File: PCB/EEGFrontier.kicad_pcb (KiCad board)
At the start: 2 copper layers, 55 x 41.5 mm, 33 parts, among them J1 Conn_01x08_Pin, SW1 SW_Push, U1 102010428, U2 ADS1299-4PAGR

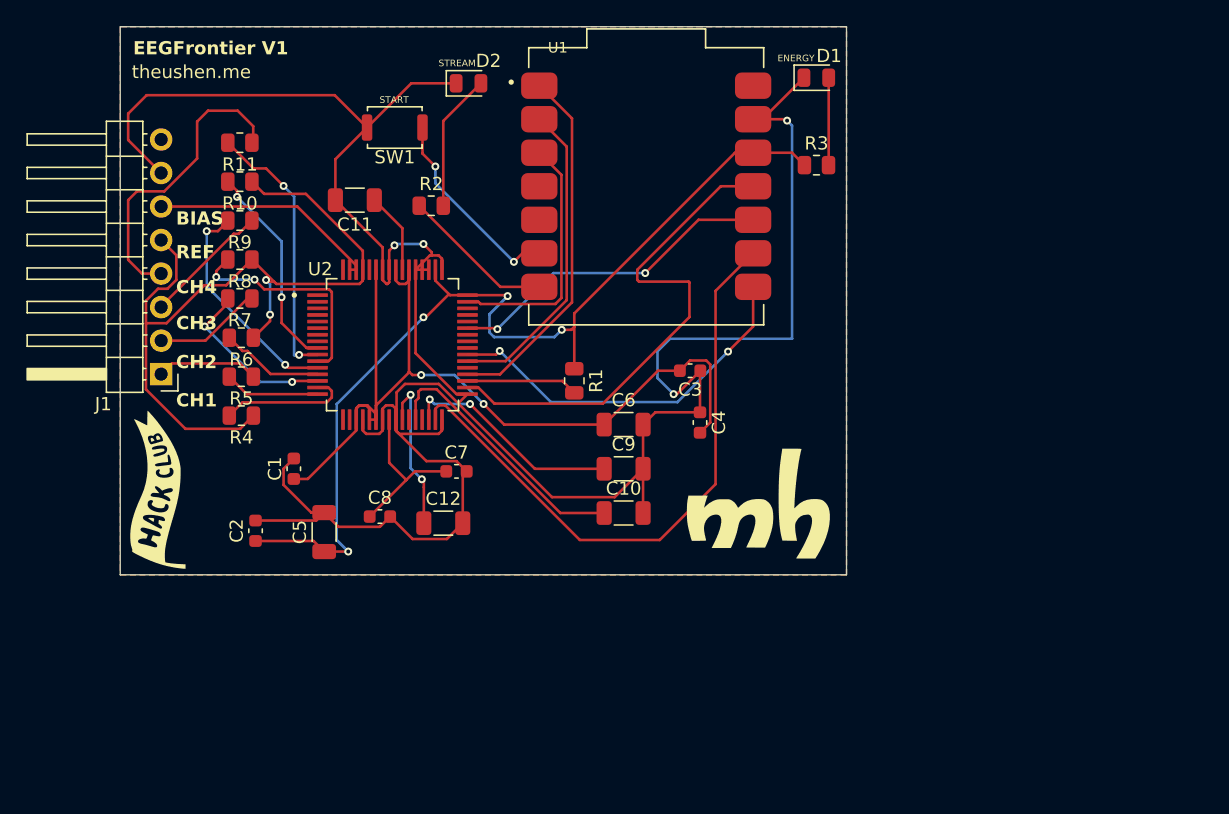
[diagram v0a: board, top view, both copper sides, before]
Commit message: feat(hw): launch EEGFrontier V2 with ADS1299IPAGR and 8-channel PCB update
- migrate analog front-end from ADS1299-4PAGR (V1) to ADS1299IPAGR (V2)
- expand hardware target from 4 EEG channels to 8 channels
- apply PCB noise-reduction rework:
  - reduce direct GND trace routing in sensitive analog areas
  - adopt curved track routing for cleaner analog paths
- update KiCad design artifacts (PCB/SCH) and generated fabrication outputs
- add V2 hardware assets (3D front/back, PCB view)
- refresh README with V1 vs V2 comparisons and updated project status

TODO (next steps):
- update BOM for V2 components and pricing
- update/validate firmware for V2 hardware revision

Refs #4
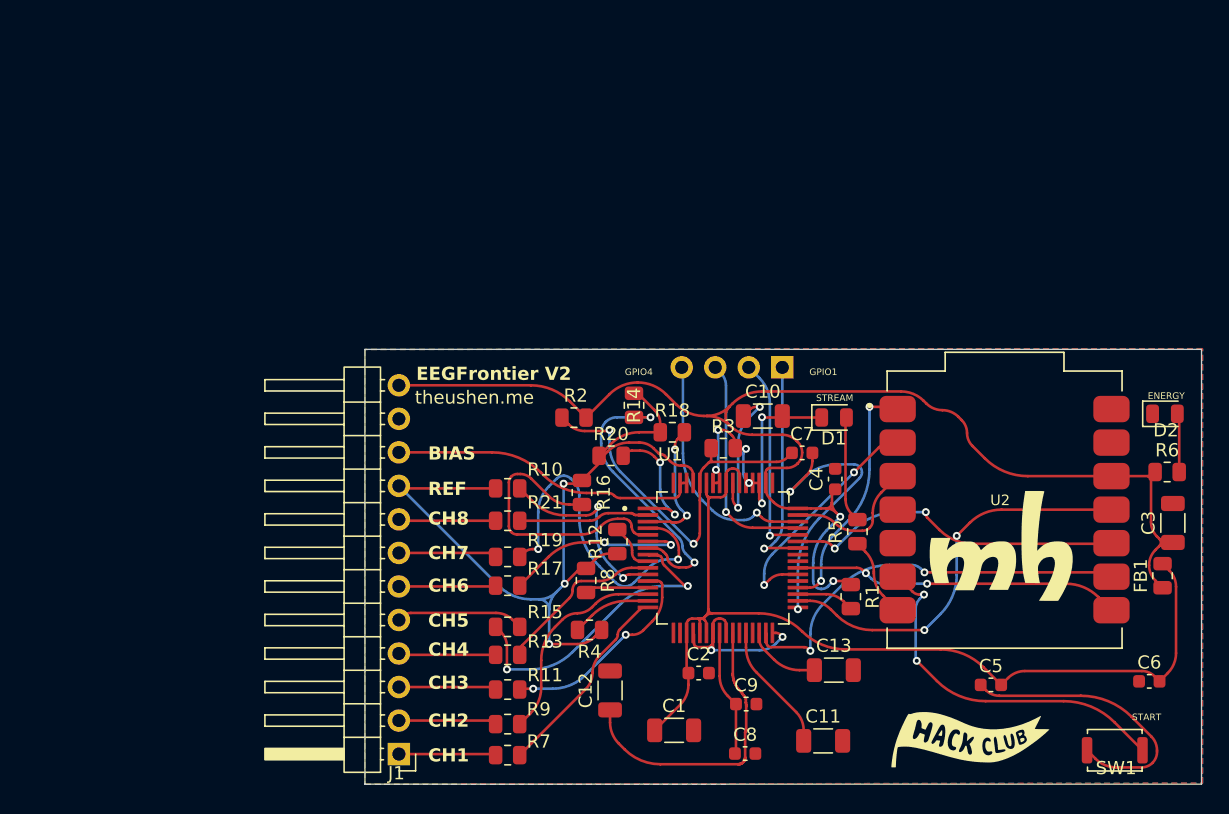
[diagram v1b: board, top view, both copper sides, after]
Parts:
- removed G*** (x4): LOGO, LOGO
- added C13: 10µF, Capacitor_SMD:C_1206_3216Metric, F.Cu at (161.1, 109.8)
- added FB1: 600Ω 100 MHz, Resistor_SMD:R_0805_2012Metric, F.Cu at (186.0, 102.6)
- added G1: LOGO, LOGO, F.Cu at (173.9, 101.6)
- added G2: LOGO, LOGO, B.Cu at (173.4, 103.2)
- added G3: LOGO, LOGO, B.Cu at (141.1, 104.0)
- added G4: LOGO, LOGO, F.Cu at (171.4, 115.0)
- added J2: Expansion, Connector_PinHeader_2.54mm:PinHeader_1x04_P2.54mm_Horizontal, B.Cu at (157.2, 86.8)
- added R12: 100k, Resistor_SMD:R_0805_2012Metric, F.Cu at (144.7, 100.0)
- added R13: 100k, Resistor_SMD:R_0805_2012Metric, F.Cu at (136.4, 108.6)
- added R14: 100k, Resistor_SMD:R_0805_2012Metric, F.Cu at (145.9, 89.7)
- added R15: 100k, Resistor_SMD:R_0805_2012Metric, F.Cu at (136.4, 106.5)
- added R16: 100k, Resistor_SMD:R_0805_2012Metric, F.Cu at (142.0, 96.3)
- added R17: 100k, Resistor_SMD:R_0805_2012Metric, F.Cu at (136.4, 103.4)
- added R18: 100k, Resistor_SMD:R_0805_2012Metric, F.Cu at (148.8, 91.7)
- added R19: 100k, Resistor_SMD:R_0805_2012Metric, F.Cu at (136.4, 101.2)
- added R20: 100k, Resistor_SMD:R_0805_2012Metric, F.Cu at (144.2, 93.5)
- added R21: 100k, Resistor_SMD:R_0805_2012Metric, F.Cu at (136.4, 98.4)
- C1, C3: value 100nF -> 10µF; footprint Capacitor_SMD:C_0603_1608Metric -> Capacitor_SMD:C_1206_3216Metric
- C5, C6, C9: value 10µF -> 100nF; footprint Capacitor_SMD:C_1206_3216Metric -> Capacitor_SMD:C_0603_1608Metric
- C7: value 100nF -> 1µF
- J1: value Conn_01x08_Pin -> Conn_01x12_Pin; footprint Connector_PinHeader_2.54mm:PinHeader_1x08_P2.54mm_Horizontal -> Connector_PinHeader_2.54mm:PinHeader_1x12_P2.54mm_Horizontal
- R2, R3: value 1kΩ -> 10k
- R5, R6: value 100k -> 1kΩ
- U1: value 102010428 -> ADS1299IPAGR; footprint OPL:MODULE_102010428 -> OPL:QFP50P1200X1200X120-64N
- U2: value ADS1299-4PAGR -> 102010428; footprint OPL:QFP50P1200X1200X120-64N -> OPL:MODULE_102010428
- moved SW1 72.1 mm to (182.3, 115.8)
- moved R6 70.9 mm to (186.3, 94.8), turned to 0 degrees
- moved D2 58.4 mm to (186.2, 90.3)
- moved C11 54.2 mm to (160.3, 115.1), turned to 0 degrees
- moved C5 51.8 mm to (173.0, 110.9), turned to 0 degrees
- moved R5 48.1 mm to (162.9, 99.3), turned to 90 degrees
- moved U2 48.0 mm to (174.0, 97.6)
- moved R11 46.1 mm to (136.4, 111.2), turned to 0 degrees
- moved C6 44.3 mm to (185.0, 110.6)
- moved R9 43.2 mm to (136.4, 113.8), turned to 0 degrees
- moved R7 40.1 mm to (136.4, 116.2), turned to 0 degrees
- moved C3 38.4 mm to (186.8, 98.6), turned to 90 degrees
- moved R8 35.8 mm to (142.3, 103.0), turned to -90 degrees
- moved C2 35.3 mm to (150.8, 110.0), turned to 0 degrees
- moved C1 35.0 mm to (149.0, 114.3), turned to 0 degrees
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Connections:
- C10 pad 1: Net-(U2-VCAP1) -> Net-(U1-VCAP3)
- C11 pad 1: Net-(U2-VCAP3) -> Net-(U1-VCAP1)
- C12 pad 1: Net-(U2-VCAP4) -> Net-(U1-VCAP4)
- C2 pad 1: 3V3_D -> 3V3_A
- C3 pad 1: GND -> 3V3_D
- C3 pad 2: 3V3_A -> GND
- C4 pad 1: GND -> 3V3_D
- C4 pad 2: 3V3_A -> GND
- C5 pad 1: 3V3_D -> GND
- C5 pad 2: GND -> 3V3_A
- C6 pad 1: 3V3_A -> GND
- C6 pad 2: GND -> 3V3_A
- C7 pad 1: Net-(U2-VREFP) -> Net-(U1-BIASREF)
- C8 pad 1: Net-(U2-VREFP) -> Net-(U1-VREFP)
- C9 pad 1: Net-(U2-VCAP2) -> Net-(U1-VREFP)
- J1 pad 5: EEG_REF -> EEG_CH5
- J1 pad 6: EEG_BIAS -> EEG_CH6
- J1 pad 7: GND -> EEG_CH7
- J1 pad 8: unconnected-(J1-Pin_8-Pad8) -> EEG_CH8
- R1 pad 2: Net-(U2-~{PWDN}) -> Net-(U1-~{PWDN})
- R10 pad 2: Net-(U2-IN4N) -> Net-(U1-IN3N)
- R11 pad 1: EEG_CH4 -> EEG_CH3
- R11 pad 2: Net-(U2-IN4P) -> Net-(U1-IN3P)
- R2 pad 1: LED_STREAM -> Net-(U1-BIASREF)
- R2 pad 2: Net-(D2-A) -> 3V3_D
- R3 pad 1: 3V3_D -> Net-(U1-BIASREF)
- R3 pad 2: Net-(D1-A) -> GND
- R4 pad 2: Net-(U2-IN1N) -> Net-(U1-IN1N)
- R5 pad 1: EEG_CH1 -> LED_STREAM
- R5 pad 2: Net-(U2-IN1P) -> Net-(D1-A)
- R6 pad 1: EEG_REF -> 3V3_D
- R6 pad 2: Net-(U2-IN2N) -> Net-(D2-A)
- R7 pad 1: EEG_CH2 -> EEG_CH1
- R7 pad 2: Net-(U2-IN2P) -> Net-(U1-IN1P)
- R8 pad 2: Net-(U2-IN3N) -> Net-(U1-IN2N)
- R9 pad 1: EEG_CH3 -> EEG_CH2
- R9 pad 2: Net-(U2-IN3P) -> Net-(U1-IN2P)
- U1 pad 1: EEG_RESET -> Net-(U1-IN8N)
- U1 pad 10: SPI_MISO -> Net-(U1-IN4P)
- U1 pad 11: SPI_MOSI -> Net-(U1-IN3N)
- U1 pad 12: 3V3_D -> Net-(U1-IN3P)
- U1 pad 13: GND -> Net-(U1-IN2N)
- U1 pad 14: VBUS -> Net-(U1-IN2P)
- U1 pad 2: EEG_START -> Net-(U1-IN8P)
- U1 pad 3: EEG_DRDY -> Net-(U1-IN7N)
- U1 pad 4: unconnected-(U1-P29/A3/D3-Pad4) -> Net-(U1-IN7P)
- U1 pad 5: unconnected-(U1-P6/SDA/D4-Pad5) -> Net-(U1-IN6N)
- U1 pad 6: BTN_START -> Net-(U1-IN6P)
- U1 pad 7: LED_STREAM -> Net-(U1-IN5N)
- U1 pad 8: SPI_CS -> Net-(U1-IN5P)
- U1 pad 9: SPI_SCK -> Net-(U1-IN4N)
- U2 pad 1: unconnected-(U2-IN8N-Pad1) -> EEG_RESET
- U2 pad 10: Net-(U2-IN4P) -> SPI_MISO
- U2 pad 11: Net-(U2-IN3N) -> SPI_MOSI
- U2 pad 12: Net-(U2-IN3P) -> 3V3_D
- U2 pad 13: Net-(U2-IN2N) -> GND
- U2 pad 14: Net-(U2-IN2P) -> VBUS
- U2 pad 2: unconnected-(U2-IN8P-Pad2) -> EEG_START
- U2 pad 3: unconnected-(U2-IN7N-Pad3) -> EEG_DRDY
- U2 pad 6: unconnected-(U2-IN6P-Pad6) -> BTN_START
- U2 pad 7: unconnected-(U2-IN5N-Pad7) -> LED_STREAM
- U2 pad 8: unconnected-(U2-IN5P-Pad8) -> SPI_CS
- U2 pad 9: Net-(U2-IN4N) -> SPI_SCK
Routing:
- net GND: track 200.2 -> 82.5 mm, vias 4 -> 10
- net 3V3_D: track 74.9 -> 107.6 mm, vias 4 -> 2
- net Net-(U1-BIASREF): track 0.00 -> 29.4 mm, vias 0 -> 2
- net Net-(U1-IN7P): track 0.00 -> 27.0 mm, vias 0 -> 2
- net Net-(U1-IN5P): track 0.00 -> 23.6 mm, vias 0 -> 2
- net Net-(U1-VCAP4): track 0.00 -> 22.8 mm
- net Net-(U1-IN5N): track 0.00 -> 22.5 mm, vias 0 -> 2
- net Net-(U1-IN6N): track 0.00 -> 21.9 mm
- net Net-(U2-IN4P): track 20.5 -> 0.00 mm, vias 2 -> 0
- net Net-(U2-VCAP1): track 20.2 -> 0.00 mm
- net /ADS_GPIO4: track 0.00 -> 18.6 mm, vias 0 -> 1
- net Net-(U2-IN3N): track 17.1 -> 0.00 mm, vias 2 -> 0
- net /ADS_GPIO3: track 0.00 -> 17.1 mm, vias 0 -> 1
- net Net-(U2-IN3P): track 17.1 -> 0.00 mm, vias 2 -> 0
- net Net-(U2-VCAP2): track 16.9 -> 0.00 mm, vias 2 -> 0
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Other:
- board size 55 x 41.5 mm -> 63.4 x 32.9 mm
- board text added: "CH5"
- board text added: "CH6"
- board text added: "CH7"
- board text added: "CH8"
- board text added: "EEGFrontier V2"
- board text added: "GPIO1"
- board text added: "GPIO4"
- board text removed: "EEGFrontier V1"
